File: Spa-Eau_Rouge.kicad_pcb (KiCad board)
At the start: 2 copper layers, 3 parts, among them U1 XIAO-ESP32-C3-SMD

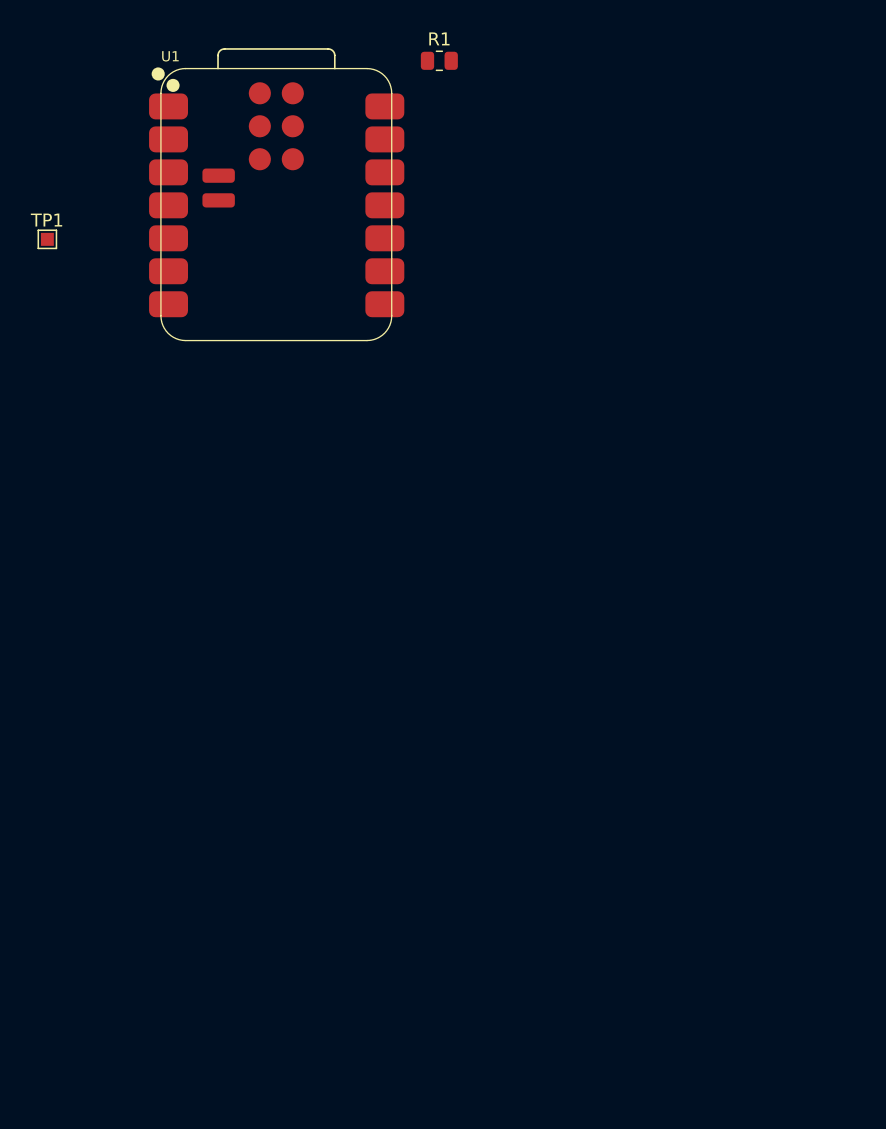
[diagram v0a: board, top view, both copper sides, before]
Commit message: drew buck circuit
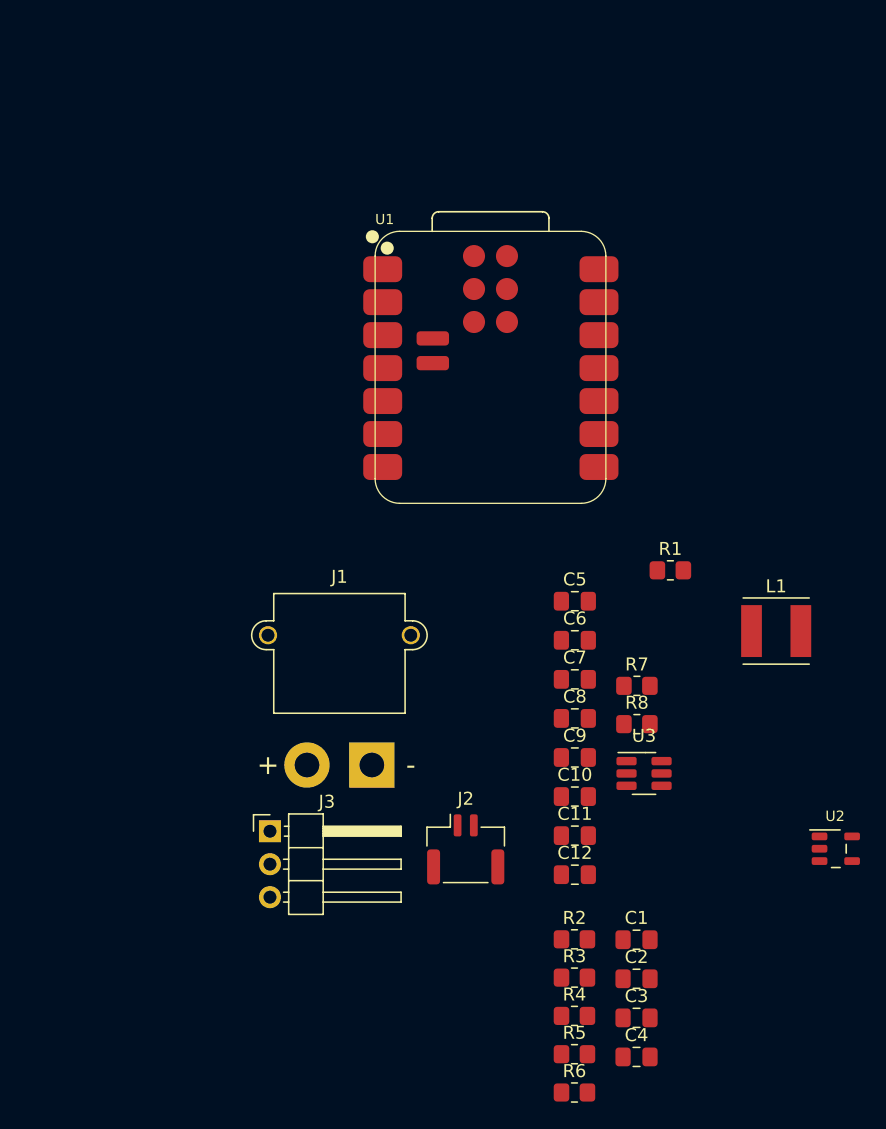
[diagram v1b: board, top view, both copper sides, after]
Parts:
- removed TP1: TestPoint, TestPoint:TestPoint_Pad_1.0x1.0mm
- added C1: CL21B104KBCNNNC, Capacitor_SMD:C_0805_2012Metric_Pad1.18x1.45mm_HandSolder, F.Cu at (87.4, 96.5)
- added C10: GRM21BR61C106KE15K, Capacitor_SMD:C_0805_2012Metric_Pad1.18x1.45mm_HandSolder, F.Cu at (82.6, 85.4)
- added C11: GRM21BR61C106KE15K, Capacitor_SMD:C_0805_2012Metric_Pad1.18x1.45mm_HandSolder, F.Cu at (82.6, 88.4)
- added C12: GRM21BR61C106KE15K, Capacitor_SMD:C_0805_2012Metric_Pad1.18x1.45mm_HandSolder, F.Cu at (82.6, 91.5)
- added C2: CL21B105KAFNNNE, Capacitor_SMD:C_0805_2012Metric_Pad1.18x1.45mm_HandSolder, F.Cu at (87.4, 99.5)
- added C3: CL21B104KBCNNNC, Capacitor_SMD:C_0805_2012Metric_Pad1.18x1.45mm_HandSolder, F.Cu at (87.4, 102.5)
- added C4: CL21B104KBCNNNC, Capacitor_SMD:C_0805_2012Metric_Pad1.18x1.45mm_HandSolder, F.Cu at (87.4, 105.5)
- added C5: CL21B104KBCNNNC, Capacitor_SMD:C_0805_2012Metric_Pad1.18x1.45mm_HandSolder, F.Cu at (82.6, 70.4)
- added C6: GRM21BR61C106KE15K, Capacitor_SMD:C_0805_2012Metric_Pad1.18x1.45mm_HandSolder, F.Cu at (82.6, 73.4)
- added C7: GRM21BR61H475KE51L, Capacitor_SMD:C_0805_2012Metric_Pad1.18x1.45mm_HandSolder, F.Cu at (82.6, 76.4)
- added C8: GRM21BR61H475KE51L, Capacitor_SMD:C_0805_2012Metric_Pad1.18x1.45mm_HandSolder, F.Cu at (82.6, 79.4)
- added C9: CL21B104KBCNNNC, Capacitor_SMD:C_0805_2012Metric_Pad1.18x1.45mm_HandSolder, F.Cu at (82.6, 82.4)
- added J1: XT30PW-M, Connector_AMASS:AMASS_XT30PW-M_1x02_P2.50mm_Horizontal, F.Cu at (67.0, 83.0)
- added J2: SM02B-GHS-TB, Connector_JST:JST_GH_SM02B-GHS-TB_1x02-1MP_P1.25mm_Horizontal, F.Cu at (74.2, 89.5)
- added J3: PH1RA-03-UA, Connector_PinHeader_2.54mm:PinHeader_1x03_P2.54mm_Horizontal, F.Cu at (59.1, 88.1)
- added L1: NRS5030T4R7MMGJV, Inductor_SMD:L_Taiyo-Yuden_NRS5030T4R7MMGJV, F.Cu at (98.2, 72.7)
- added R2: DNP 0805, Resistor_SMD:R_0805_2012Metric_Pad1.20x1.40mm_HandSolder, F.Cu at (82.6, 96.4)
- added R3: RMCF0805JT4K70, Resistor_SMD:R_0805_2012Metric_Pad1.20x1.40mm_HandSolder, F.Cu at (82.6, 99.4)
- added R4: DNP 0805, Resistor_SMD:R_0805_2012Metric_Pad1.20x1.40mm_HandSolder, F.Cu at (82.6, 102.3)
- added R5: RC0805JR-070RL, Resistor_SMD:R_0805_2012Metric_Pad1.20x1.40mm_HandSolder, F.Cu at (82.6, 105.3)
- added R6: DNP 0805, Resistor_SMD:R_0805_2012Metric_Pad1.20x1.40mm_HandSolder, F.Cu at (82.6, 108.2)
- added R7: ERA-6AEB114V, Resistor_SMD:R_0805_2012Metric_Pad1.20x1.40mm_HandSolder, F.Cu at (87.4, 76.9)
- added R8: RT0805BRD0715KL, Resistor_SMD:R_0805_2012Metric_Pad1.20x1.40mm_HandSolder, F.Cu at (87.4, 79.8)
- added U2: SN74LVC1G17DBVR, Package_TO_SOT_SMD:SOT-23-5_SN74LVC1G17DBVR, F.Cu at (102.7, 89.5)
- added U3: LMR51420YDDCR, Package_TO_SOT_SMD:SOT-23-6_LMR51420YDDCR, F.Cu at (88.0, 83.7)
- R1: value 0Ω -> RC0805JR-070RL; footprint Resistor_SMD:R_0805_2012Metric -> Resistor_SMD:R_0805_2012Metric_Pad1.20x1.40mm_HandSolder
- U1: value XIAO-ESP32-C3-SMD -> 113991054
- moved R1 43.1 mm to (90.0, 68.0)
- moved U1 20.7 mm to (76.1, 52.4)
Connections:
- R1 pad 1: unconnected-(R1-Pad1) -> /RELEASE_TRIGGER
- R1 pad 2: unconnected-(R1-Pad2) -> /MCU/RELEASE_TRIGGER
- U1 pad 1: PAYLOAD_RELEASE_TRIGGER -> /MCU/RELEASE_TRIGGER
- U1 pad 12: unconnected-(U1-3V3-Pad12) -> +3.3V
- U1 pad 13: unconnected-(U1-GND-Pad13) -> GND
- U1 pad 14: unconnected-(U1-5V-Pad14) -> +5V
- U1 pad 19: unconnected-(U1-CHIP_EN-Pad19) -> /MCU/CHIP_EN
- U1 pad 2: PAYLOAD_DROP_SERVO_PWM -> /MCU/RAW_SERVO_PWM
- U1 pad 20: unconnected-(U1-GND-Pad20) -> GND
- U1 pad 5: Net-(U1-GPIO6_D4_SDA) -> unconnected-(U1-GPIO6_D4_SDA-Pad5)

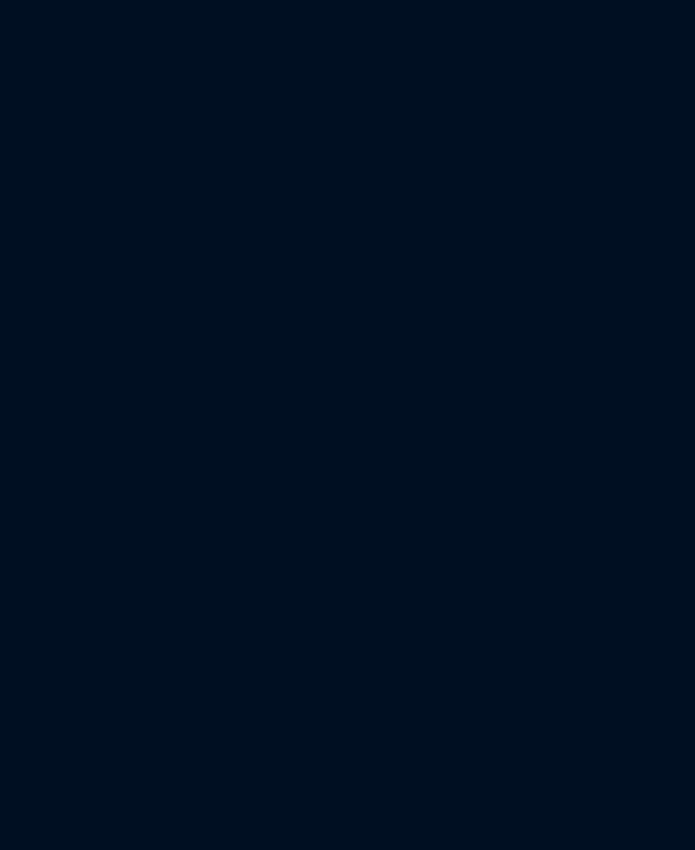
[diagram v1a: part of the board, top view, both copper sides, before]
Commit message: added CMC, TVS diode, electrolytic cap at buck input to improve inrush current effects
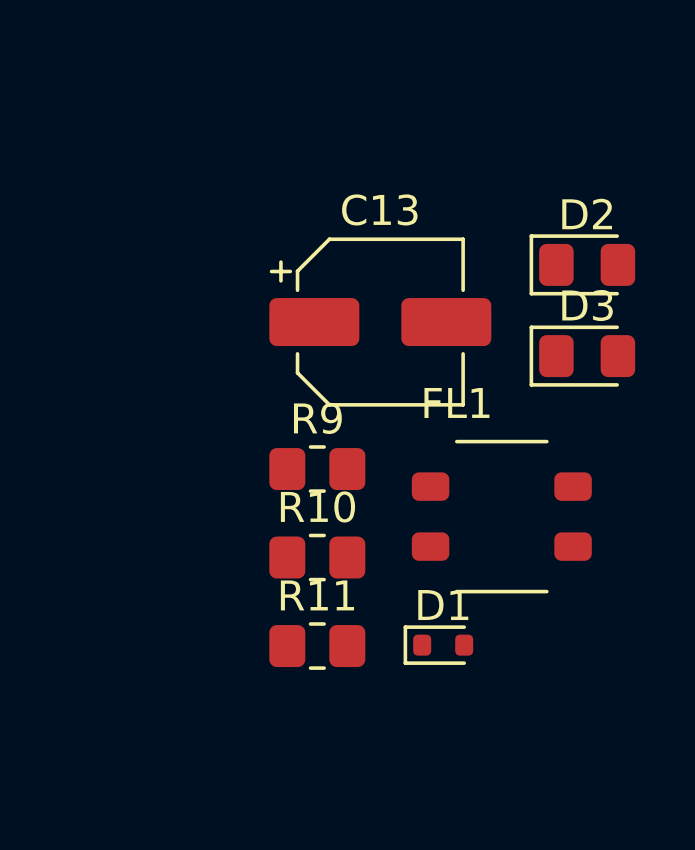
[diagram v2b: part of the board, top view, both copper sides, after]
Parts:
- added C13: 865080642006, Capacitor_SMD:865080642006, F.Cu at (160.6, 68.7)
- added D1: D24V0S1U2TQ-7, Diode_SMD:D_SOD-523, F.Cu at (162.7, 79.5)
- added D2: 150080GS75000, LED_SMD:LED_0805_2012Metric_Pad1.15x1.40mm_HandSolder, F.Cu at (167.5, 66.8)
- added D3: 150080GS75000, LED_SMD:LED_0805_2012Metric_Pad1.15x1.40mm_HandSolder, F.Cu at (167.5, 69.8)
- added FL1: ACM4520-421-2P-T000, Inductor_SMD:L_CommonModeChoke_TDK_ACM4520-421-2P-T000, F.Cu at (164.7, 75.2)
- added R10: ERJ-P06J112V, Resistor_SMD:R_0805_2012Metric_Pad1.20x1.40mm_HandSolder, F.Cu at (158.5, 76.5)
- added R11: RC0805FR-0790R9L, Resistor_SMD:R_0805_2012Metric_Pad1.20x1.40mm_HandSolder, F.Cu at (158.5, 79.5)
- added R9: RC0805JR-070RL, Resistor_SMD:R_0805_2012Metric_Pad1.20x1.40mm_HandSolder, F.Cu at (158.5, 73.6)
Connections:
- C7 pad 1: VBAT -> VBAT_FILTERED
- C8 pad 1: VBAT -> VBAT_FILTERED
- C9 pad 1: VBAT -> VBAT_FILTERED
- J1 pad 1: GND -> -BATT
- J1 pad 2: VBAT -> +BATT
- U3 pad 3: VBAT -> VBAT_FILTERED
- U3 pad 5: VBAT -> Net-(U3-EN)

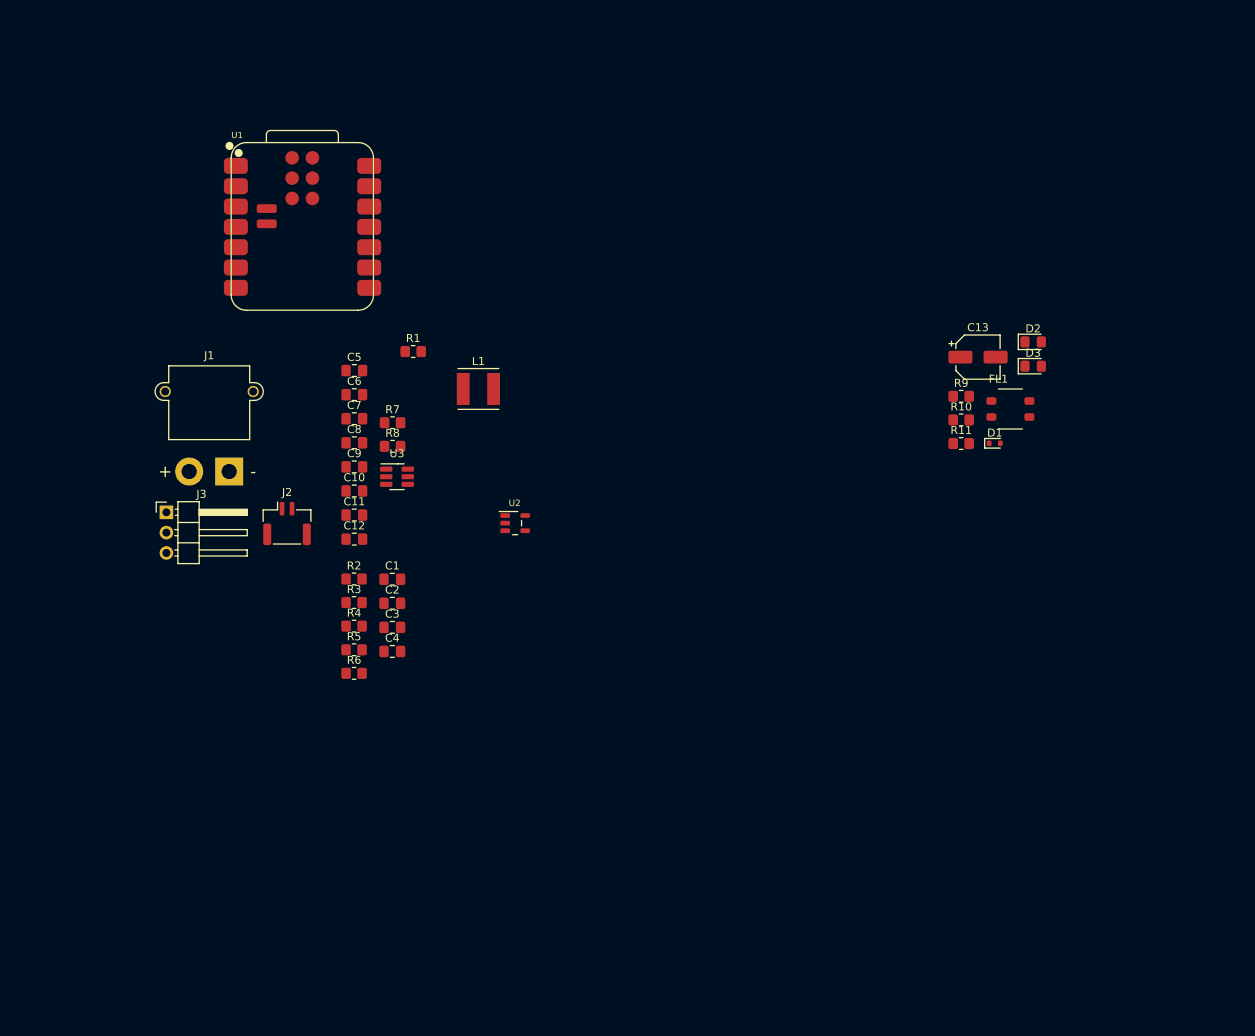
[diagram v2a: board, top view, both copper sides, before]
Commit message: 1st round of rough component placement
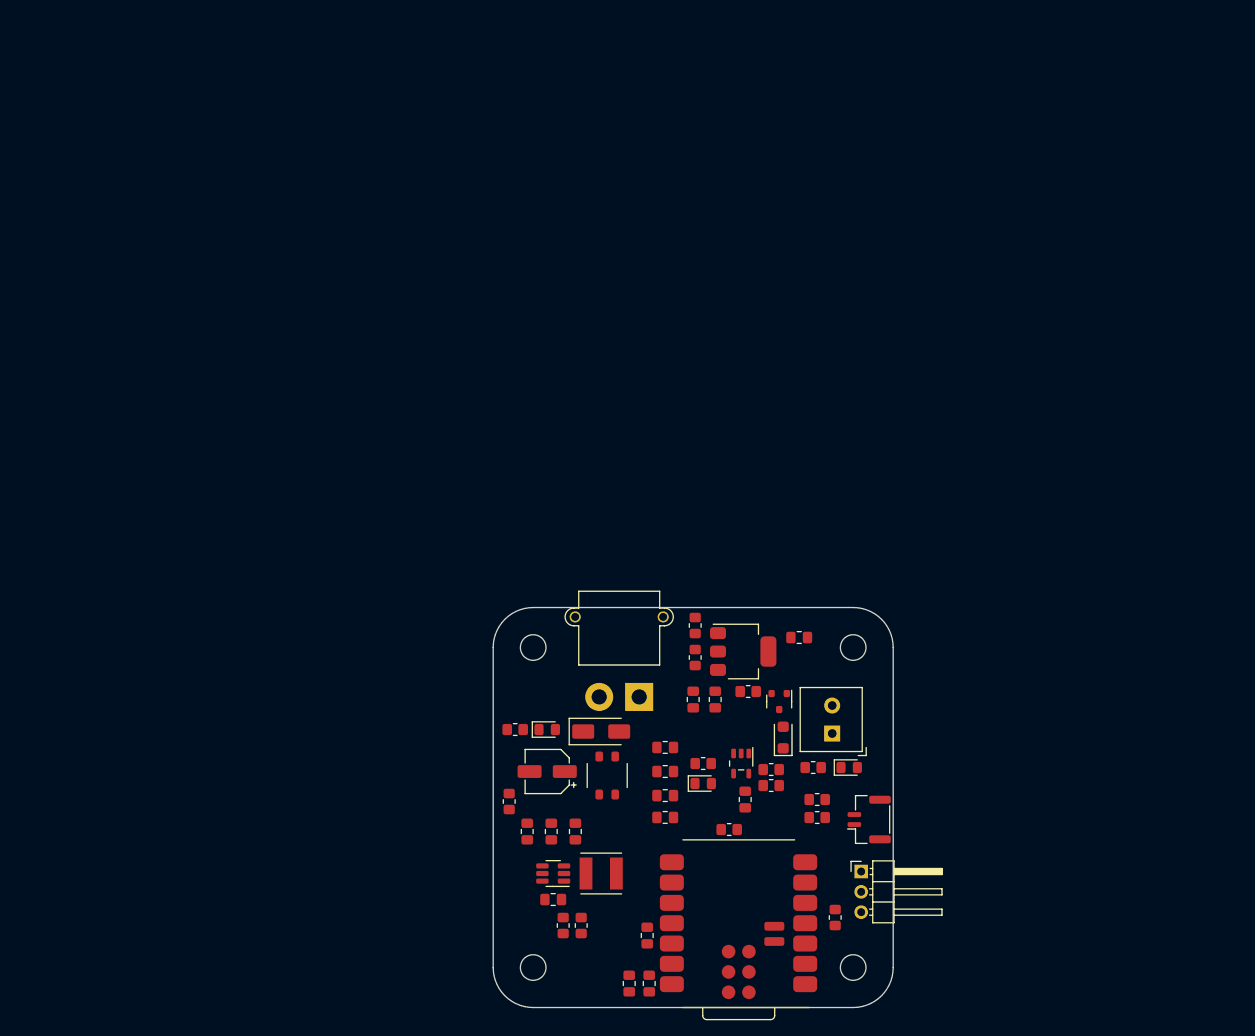
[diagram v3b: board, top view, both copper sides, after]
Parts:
- added C14: GRM21BR61H475KE51L, Capacitor_SMD:C_0805_2012Metric_Pad1.18x1.45mm_HandSolder, F.Cu at (127.8, 111.5)
- added C15: CL21B104KBCNNNC, Capacitor_SMD:C_0805_2012Metric_Pad1.18x1.45mm_HandSolder, F.Cu at (125.0, 111.5)
- added C16: GRM21BR61H475KE51L, Capacitor_SMD:C_0805_2012Metric_Pad1.18x1.45mm_HandSolder, F.Cu at (138.2, 103.8)
- added D4: 150080GS75000, LED_SMD:LED_0805_2012Metric_Pad1.15x1.40mm_HandSolder, F.Cu at (144.5, 120.0)
- added D5: STPS2H100ZF, Diode_SMD:D_SOD-123F_STPS2H100ZF, F.Cu at (136.2, 116.2)
- added H1: MountingHole, MountingHole:MountingHole_3.2mm_M3, F.Cu at (105.0, 105.0)
- added H2: MountingHole, MountingHole:MountingHole_3.2mm_M3, F.Cu at (145.0, 105.0)
- added H3: MountingHole, MountingHole:MountingHole_3.2mm_M3, F.Cu at (105.0, 145.0)
- added H4: MountingHole, MountingHole:MountingHole_3.2mm_M3, F.Cu at (145.0, 145.0)
- added J4: 1985807, TerminalBlock_Phoenix:TerminalBlock_Phoenix_MKDS-1,5-2_1x02_P3.50mm_Horizontal_1985807, F.Cu at (142.4, 115.8)
- added Q1: DMN3731U-7, Package_TO_SOT_SMD:SOT-23-3_DMN3731U-7, F.Cu at (135.8, 111.8)
- added R12: RT0805BRD071K3L, Resistor_SMD:R_0805_2012Metric_Pad1.20x1.40mm_HandSolder, F.Cu at (125.2, 106.2)
- added R13: ERJ-P06J112V, Resistor_SMD:R_0805_2012Metric_Pad1.20x1.40mm_HandSolder, F.Cu at (140.0, 120.0)
- added R14: RT0805BRD0710K7L, Resistor_SMD:R_0805_2012Metric_Pad1.20x1.40mm_HandSolder, F.Cu at (125.2, 102.2)
- added R15: RC0805JR-070RL, Resistor_SMD:R_0805_2012Metric_Pad1.20x1.40mm_HandSolder, F.Cu at (131.9, 110.5)
- added U4: LM317MDCYR, Package_TO_SOT_SMD:SOT-223-3_TabPin2_LM317MDCYR, F.Cu at (131.2, 105.5)
- C13: value 865080642006 -> GRM21BR61C106KE15K; footprint Capacitor_SMD:865080642006 -> Capacitor_SMD:C_0805_2012Metric_Pad1.18x1.45mm_HandSolder
- C5: value CL21B104KBCNNNC -> 865080642006; footprint Capacitor_SMD:C_0805_2012Metric_Pad1.18x1.45mm_HandSolder -> Capacitor_SMD:865080642006
- C6: value GRM21BR61C106KE15K -> CL21B104KBCNNNC
- D1: value D24V0S1U2TQ-7 -> 150080GS75000; footprint Diode_SMD:D_SOD-523 -> LED_SMD:LED_0805_2012Metric_Pad1.15x1.40mm_HandSolder
- D2: value 150080GS75000 -> SMAJ26A-13-F; footprint LED_SMD:LED_0805_2012Metric_Pad1.15x1.40mm_HandSolder -> Diode_SMD:D_SMAJ26A-13-F
- J2: value SM02B-GHS-TB -> PH1RA-03-UA; footprint Connector_JST:JST_GH_SM02B-GHS-TB_1x02-1MP_P1.25mm_Horizontal -> Connector_PinHeader_2.54mm:PinHeader_1x03_P2.54mm_Horizontal
- J3: value PH1RA-03-UA -> SM02B-GHS-TB; footprint Connector_PinHeader_2.54mm:PinHeader_1x03_P2.54mm_Horizontal -> Connector_JST:JST_GH_SM02B-GHS-TB_1x02-1MP_P1.25mm_Horizontal
- R10: value ERJ-P06J112V -> RC0805FR-0790R9L
- R11: value RC0805FR-0790R9L -> RT0805BRD0715KL
- R7: value ERA-6AEB114V -> ERJ-P06J112V
- R8: value RT0805BRD0715KL -> RC0805JR-070RL
- R9: value RC0805JR-070RL -> ERA-6AEB114V
- moved U1 102.9 mm to (130.8, 139.5), turned to 180 degrees
- moved J3 95.9 mm to (147.0, 126.5), turned to 90 degrees
- moved J2 83.9 mm to (146.0, 133.0)
- moved R9 82.8 mm to (108.8, 139.8), turned to 90 degrees
- moved R1 77.1 mm to (140.5, 126.2)
- moved R11 76.7 mm to (111.0, 139.8), turned to -90 degrees
- moved D2 72.7 mm to (113.5, 115.5)
- moved C13 69.6 mm to (121.5, 126.2)
- moved FL1 68.1 mm to (114.2, 121.0), turned to 90 degrees
- moved C6 67.8 mm to (107.5, 136.5)
- moved R6 67.4 mm to (142.8, 138.8), turned to 90 degrees
- moved D3 66.5 mm to (126.2, 122.0)
- moved D1 66.4 mm to (106.8, 115.2)
- moved R2 64.1 mm to (140.5, 124.0)
- moved L1 62.5 mm to (113.5, 133.2)
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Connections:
- net /MCU/RELEASE_TRIGGER renamed /MCU/RELEASE_TRIGGER_3.3V
- C13 pad 1: VBAT_FILTERED -> +5V
- C5 pad 1: Net-(U3-CB) -> VBAT_FILTERED
- C5 pad 2: Net-(U3-SW) -> GND
- C6 pad 1: +5V -> /Power/BOOT
- C6 pad 2: GND -> /Power/SW
- D1 pad 1: +BATT -> /Power/VIN_LED_K
- D1 pad 2: -BATT -> VBAT_FILTERED
- D2 pad 1: Net-(D2-K) -> +BATT
- D2 pad 2: VBAT_FILTERED -> -BATT
- D3 pad 1: Net-(D3-K) -> /Power/5V_LED_K
- J2 pad 1: /RELEASE_TRIGGER -> /BUFF_SERVO_PWM
- J2 pad 2: GND -> +5V
- J3 pad 1: /BUFF_SERVO_PWM -> /RELEASE_TRIGGER
- J3 pad 2: +5V -> GND
- L1 pad 1: Net-(U3-SW) -> /Power/SW
- R10 pad 1: Net-(D2-K) -> /Power/5V_LED_K
- R11 pad 1: Net-(D3-K) -> /Power/FB
- R7 pad 1: +5V -> /Power/VIN_LED_K
- R7 pad 2: Net-(U3-FB) -> GND
- R8 pad 1: Net-(U3-FB) -> VBAT_FILTERED
- R8 pad 2: GND -> /Power/EN
- R9 pad 1: VBAT_FILTERED -> +5V
- R9 pad 2: Net-(U3-EN) -> /Power/FB
- U1 pad 3: unconnected-(U1-GPIO4_A2_D2-Pad3) -> /SOLENOID_DRIVE
- U3 pad 2: Net-(U3-SW) -> /Power/SW
- U3 pad 4: Net-(U3-FB) -> /Power/FB
- U3 pad 5: Net-(U3-EN) -> /Power/EN
- U3 pad 6: Net-(U3-CB) -> /Power/BOOT
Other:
- board outline added: 50 x 50 mm
- copper layers 2 -> 4
- board text added: "${REFERENCE}"
